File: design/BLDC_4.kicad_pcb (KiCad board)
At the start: 4 copper layers, 38.5 x 65 mm, 126 parts, among them K1 SERVO, P1 HALL/Encoder, P101 CANBUS, P2 SWD, P3 PWR_COMM, P4 IN+, P5 IN-, P6 MOTOR1, P7 MOTOR2, P9 MOTOR3, Q1 IRFS7530, Q2 IRFS7530, Q3 IRFS7530, Q4 IRFS7530, Q5 IRFS7530, Q6 IRFS7530, U1 STM32F40X_LQFP64, U2 TC2117, U3 DRV8302, U401 SN65HVD232, X1 MINI-USB-SHIELD-32005-201, X2 8MHz 10ppm

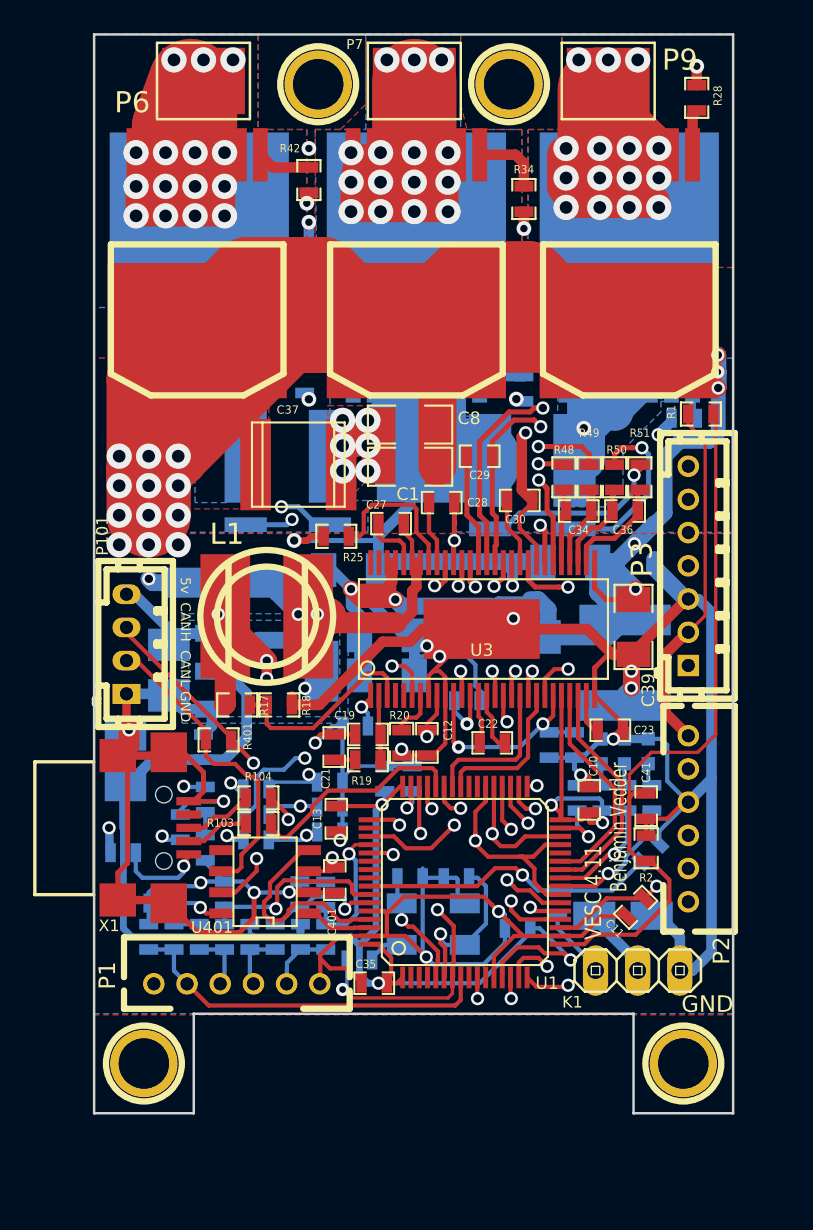
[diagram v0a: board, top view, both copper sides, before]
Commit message: Implemented some improvements in schematic, but layout is completely new.
Changes in schematic:
- 3.3V or 5V CAN transceiver can be used
- DRV8301 can also be used and configured via SPI
- JTAG connector changed
- Fixed pinning of P1
- Some additional decoupling and/or filtering of analog signals
- Improved buck design according TI Webench recommendation
- Changed some component values
- maybe others...

Changes in layout:
- completely new layout
- placement of the big components is unchanged
- CAN connector rotated by 180°
- kept one layer free as a good GND plane
- many traces should be shorter and have lower impedance now
- improved buck layout

Other changes:
- updated gerber files
- updated PDFs (schematic and component placement)
- deleted all outdated files except libraries and datasheets
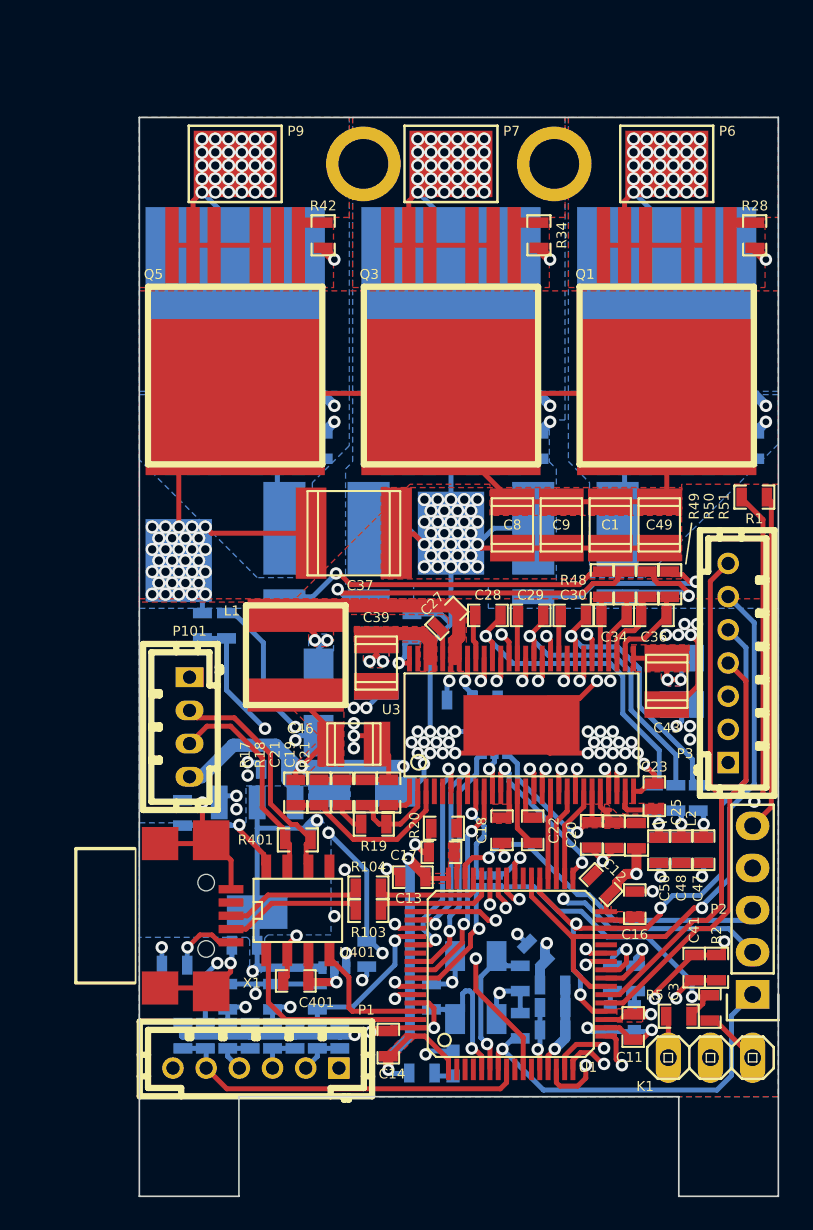
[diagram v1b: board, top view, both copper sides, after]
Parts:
- removed 1PIN (x2): P***, 1pin
- removed 1PIN (x2): P***, Connect:1pin
- removed C51: 15u, 100v, w_smd_cap:c_2220
- removed C52: 2.2u, CRF1:SMD-0603_c
- removed G***: oshw_silkscreen-back_3mm, oshw_silkscreen-back_3mm
- removed R30, R36, R46: 39k, CRF1:SMD-0603_r
- added C45: 6n8 opt, CRF1:SMD-0603_c, B.Cu at (97.7, 115.7)
- added C46: 47u,10V, w_smd_cap:c_1210, F.Cu at (94.2, 122.8)
- added C47: 100n, CRF1:SMD-0603_c, F.Cu at (115.2, 129.2)
- added C48: 100n, CRF1:SMD-0603_c, F.Cu at (113.9, 129.2)
- added C50: 100n, CRF1:SMD-0603_c, F.Cu at (112.5, 129.2)
- added JP1: JUMPER, open-project:S_JUMPER_2, B.Cu at (102.8, 131.0)
- added JP2: JUMPER, open-project:S_JUMPER_2, B.Cu at (101.8, 131.0)
- added JP3: JUMPER3, open-project:S_JUMPER_3, B.Cu at (102.6, 123.3)
- added JP4: JUMPER3, open-project:S_JUMPER_3, B.Cu at (93.0, 136.2)
- added L2: L, CRF1:SMD-0603_r, F.Cu at (111.2, 128.3)
- added L3: L, CRF1:SMD-0603_r, B.Cu at (106.1, 137.3)
- added R14: 0R, CRF1:SMD-0603_r, B.Cu at (100.5, 120.1)
- added REF**: MountingHole_3mm, Mounting_Holes:MountingHole_3mm, F.Cu at (106.8, 88.0)
- added REF**: MountingHole_3mm, Mounting_Holes:MountingHole_3mm, F.Cu at (94.2, 87.7)
- C1, C39, C40, C44, C8: value 10u,50V -> 10u,63V; footprint CRF1:SMD-1206 -> w_smd_cap:c_1210
- C10, C35, R25: moved to B.Cu
- C14, C16, C17, C3, R5: moved to F.Cu
- C18: value 2.2u -> 4.7u,25V; moved to F.Cu
- C19: value 120p -> 1p5
- C20: value 2.2u -> 2.2u,16V; moved to F.Cu
- C21: value 6.8n -> 2n
- C23: value 2.2u -> 2.2u,16V
- C25: value 100u -> 100n; footprint w_smd_cap:c_tant_B -> CRF1:SMD-0603_c; moved to F.Cu
- C33: value 100u -> 2.2u; footprint w_smd_cap:c_tant_B -> CRF1:SMD-0603_c
- C34, C36: value 2.2n -> 2n
- C37: value 15u,100V -> 22u,63V
- C43, C49, C9: value 10u,50V -> 10u,63V; footprint CRF1:SMD-1206 -> w_smd_cap:c_1210; moved to F.Cu
- D4: value DIODESCH -> Schottky; footprint Diodes_SMD:SMA_Handsoldering -> Diodes_SMD:SMA_Standard
- D5: footprint w_smd_diode:do214ac -> Diodes_SMD:SMA_Standard
- L1: value 22u -> 33u; footprint w_smd_inductors:inductor_smd_8x5mm -> pikim:inductor_smd_6x6mm
- P1: footprint CRF1:MICRO_JST_6 -> pikim:b6b-ph-kl
- P2: footprint CRF1:MICRO_JST_6 -> Pin_Headers:Pin_Header_Straight_1x05
- P3: footprint CRF1:b7b-ph-kl -> pikim:b7b-ph-kl
- Q1, Q2, Q3, Q4, Q5, Q6: footprint CRF1:D2PAK-7-GDS -> pikim:D2PAK-7-GDS
- R17: value 18k -> 52k5
- R18: value 3k3 -> 10k
- R19: value 15k -> 100k
- R21: value 220k -> 301k; moved to F.Cu
- R37, R38, R48, R49, R50, R51: value 100R -> 120R
- U3: value DRV8302 -> DRV8301/2; footprint CRF1:TSSOP-56-PP -> pikim:TSSOP-56-PP
- moved C25 29.8 mm to (109.8, 128.2), turned to 90 degrees
- moved P6 28.4 mm to (113.0, 87.8)
- moved R23 26.8 mm to (114.9, 126.0), turned to 270 degrees
- moved R26 25.3 mm to (113.5, 126.0), turned to 270 degrees
- moved R32 24.0 mm to (112.2, 126.0), turned to 270 degrees
- moved P9 23.0 mm to (87.0, 87.8)
- moved R24 22.6 mm to (115.2, 129.2), turned to 90 degrees
- moved R27 21.3 mm to (113.9, 129.2), turned to 90 degrees
- moved D3 20.8 mm to (100.1, 142.0)
- moved R33 20.2 mm to (112.5, 129.2), turned to 90 degrees
- moved C43 20.2 mm to (113.0, 119.0), turned to 90 degrees
- moved R22 19.8 mm to (98.2, 142.6), turned to 180 degrees
- moved C49 18.7 mm to (112.5, 109.5), turned to 90 degrees
- moved C44 18.0 mm to (113.9, 119.0), turned to 90 degrees
- moved R54 17.9 mm to (107.5, 112.8)
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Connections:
- C25 pad 1: VCC -> GND
- C25 pad 2: GND -> Net-(C25-Pad2)
- C31 pad 2: VCC -> Net-(C31-Pad2)
- C35 pad 2: VCC -> Net-(C31-Pad2)
- C401 pad 1: VCC -> Net-(C401-Pad1)
- D5 pad 1: GND -> +5V
- D5 pad 2: +5V -> GND
- P1 pad 1: +5V -> GND
- P1 pad 2: /Filters/TEMP_IN -> /Filters/HALL3_IN
- P1 pad 3: /Filters/HALL1_IN -> /Filters/HALL2_IN
- P1 pad 4: /Filters/HALL2_IN -> /Filters/HALL1_IN
- P1 pad 5: /Filters/HALL3_IN -> /Filters/TEMP_IN
- P1 pad 6: GND -> +5V
- P2 pad 1: VCC -> NRST
- P2 pad 3: GND -> SWDIO
- P2 pad 4: SWDIO -> GND
- P2 pad 5: NRST -> VCC
- Q1 pad S: /Mosfet driver/H1_VS -> /Mosfet driver/H3_VS
- Q2 pad D: /Mosfet driver/H1_VS -> /Mosfet driver/H3_VS
- Q2 pad S: /Mosfet driver/H1_LOW -> /Mosfet driver/H3_LOW
- Q5 pad S: /Mosfet driver/H3_VS -> /Mosfet driver/H1_VS
- Q6 pad D: /Mosfet driver/H3_VS -> /Mosfet driver/H1_VS
- Q6 pad S: /Mosfet driver/H3_LOW -> /Mosfet driver/H1_LOW
- R25 pad 1: GND -> Net-(R14-Pad1)
- R25 pad 2: Net-(R25-Pad2) -> GND
- R28 pad 2: /Mosfet driver/M_H1 -> /Mosfet driver/M_H3
- R29 pad 2: /Mosfet driver/M_L1 -> /Mosfet driver/M_L3
- R42 pad 2: /Mosfet driver/M_H3 -> /Mosfet driver/M_H1
- R43 pad 2: /Mosfet driver/M_L3 -> /Mosfet driver/M_L1
- R50 pad 2: Net-(C36-Pad1) -> Net-(C36-Pad2)
- R51 pad 2: Net-(C36-Pad2) -> Net-(C36-Pad1)
- R53 pad 1: GND -> /Mosfet driver/H1_LOW
- R53 pad 2: /Mosfet driver/H1_LOW -> GND
- R53 pad 3: /Mosfet driver/SH2_B -> /Mosfet driver/SH1_A
- R53 pad 4: /Mosfet driver/SH2_A -> /Mosfet driver/SH1_B
- R54 pad 1: /Mosfet driver/H3_LOW -> GND
- R54 pad 2: GND -> /Mosfet driver/H3_LOW
- R54 pad 3: /Mosfet driver/SH1_A -> /Mosfet driver/SH2_B
- R54 pad 4: /Mosfet driver/SH1_B -> /Mosfet driver/SH2_A
- U1 pad 11: Net-(U1-Pad11) -> (no net)
- U1 pad 13: VCC -> Net-(C31-Pad2)
- U1 pad 2: Net-(U1-Pad2) -> (no net)
- U1 pad 26: /MCU/BR_SO2 -> /Mosfet driver/BR_SO1
- U1 pad 28: Net-(U1-Pad28) -> (no net)
- U1 pad 3: Net-(U1-Pad3) -> (no net)
- U1 pad 39: Net-(U1-Pad39) -> (no net)
- U1 pad 4: Net-(U1-Pad4) -> (no net)
- U1 pad 50: Net-(U1-Pad50) -> /MCU/DRV_NSS
- U1 pad 54: Net-(U1-Pad54) -> (no net)
- U1 pad 55: Net-(U1-Pad55) -> /MCU/DRV_SCK
- U1 pad 56: Net-(U1-Pad56) -> /MCU/DRV_MISO
- U1 pad 57: /MCU/SERVO -> Net-(JP2-Pad1)
- U1 pad 9: Net-(U1-Pad9) -> (no net)
- U3 pad 10: GND -> /MCU/DRV_MISO
- U3 pad 11: Net-(C20-Pad2) -> Net-(JP3-Pad2)
- U3 pad 24: VCC -> Net-(C25-Pad2)
- U3 pad 25: /MCU/BR_SO1 -> /Mosfet driver/BR_SO1
- U3 pad 26: /MCU/BR_SO2 -> /MCU/BR_SO1
- U3 pad 30: Net-(C36-Pad2) -> Net-(C36-Pad1)
- U3 pad 31: Net-(C36-Pad1) -> Net-(C36-Pad2)
- U3 pad 4: Net-(U3-Pad4) -> (no net)
- U3 pad 49: Net-(R25-Pad2) -> Net-(R14-Pad1)
- U3 pad 5: Net-(U3-Pad5) -> (no net)
- U3 pad 55: Net-(U3-Pad55) -> (no net)
- U3 pad 8: GND -> /MCU/DRV_NSS
- U3 pad 9: VCC -> /MCU/DRV_MOSI
- U401 pad 3: VCC -> Net-(C401-Pad1)
- U401 pad 5: Net-(U401-Pad5) -> (no net)
- X1 pad 4: Net-(X1-Pad4) -> (no net)
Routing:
- net V_SUPPLY: track 290.3 -> 129.8 mm, vias 20 -> 36
- net /Mosfet driver/H3_VS: track 166.9 -> 66.0 mm, vias 18 -> 31
- net /Mosfet driver/H1_VS: track 150.6 -> 69.7 mm, vias 17 -> 31
- net /Mosfet driver/H2_VS: track 145.0 -> 65.1 mm, vias 17 -> 31
- net GND: track 397.8 -> 376.8 mm, vias 26 -> 106
- net /Mosfet driver/M_H1: track 49.8 -> 32.7 mm
- net /Mosfet driver/BR_SO1: track 0.00 -> 16.2 mm, vias 0 -> 2
- net /MCU/DRV_SCK: track 0.00 -> 14.8 mm, vias 0 -> 1
- net /Mosfet driver/H3_LOW: track 53.5 -> 39.5 mm
- net /MCU/BR_SO2: track 13.9 -> 0.00 mm
- net Net-(Q2-PadG): track 16.2 -> 2.80 mm
- net /MCU/DRV_MISO: track 0.00 -> 13.2 mm, vias 0 -> 2
- net /MCU/DRV_NSS: track 0.00 -> 12.8 mm, vias 0 -> 2
- net +5V: track 115.3 -> 103.5 mm
- net /MCU/L1: track 16.1 -> 5.31 mm, vias 2 -> 0
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- added copper zone on B.Cu, net +5V
- added copper zone on F.Cu, net +5V
- added copper zone on L2, net /Mosfet driver/H1_VS
- added copper zone on L3, net /Mosfet driver/H1_VS
- added copper zone on L2, net /Mosfet driver/H2_VS
- added copper zone on L3, net /Mosfet driver/H2_VS
- added copper zone on L2, net /Mosfet driver/H3_VS
- added copper zone on L3, net /Mosfet driver/H3_VS
- added copper zone on L2, net GND
- added copper zone on L3, net GND
- added copper zone on F.Cu, net Net-(C16-Pad1)
- added copper zone on F.Cu, net Net-(C17-Pad1)
- added copper zone on F.Cu, net Net-(C18-Pad1)
- added copper zone on F.Cu, net Net-(C20-Pad2)
- added copper zone on F.Cu, net Net-(C23-Pad2)
- added copper zone on F.Cu, net Net-(C25-Pad2)
- added copper zone on B.Cu, net Net-(C27-Pad1)
- added copper zone on F.Cu, net Net-(C27-Pad1)
- added copper zone on F.Cu, net VCC
- added copper zone on B.Cu, net V_SUPPLY
- removed copper zone on GND, net /Mosfet driver/H1_VS
- removed copper zone on GND2, net /Mosfet driver/H1_VS
- removed copper zone on GND, net /Mosfet driver/H2_VS
- removed copper zone on GND2, net /Mosfet driver/H2_VS
- removed copper zone on GND, net /Mosfet driver/H3_VS
- removed copper zone on GND2, net /Mosfet driver/H3_VS
- removed copper zone on GND, net GND
- removed copper zone on GND2, net GND
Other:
- net class Default: clearance 0.1778 -> 0.199999; trace_width 0.2032 -> 0.2; via_dia 0.8 -> 0.75; via_drill 0.5 -> 0.4
- rule trace_clearance: 0.1778 -> 0.199999
- rule trace_min: 0.2032 -> 0.2
- rule via_min_drill: 0.5 -> 0.4
- rule via_min_size: 0.8 -> 0.75
- board text added: "1"
- board text added: "2"
- board text added: "3"
- board text added: "5V"
- board text added: "GN"
- board text added: "RD"
- board text added: "SERVO"
- board text added: "VESC 4.11 pikim"
- board text removed: "3.3v"
- board text removed: "5v"
- board text removed: "VESC 4.11"

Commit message: Fixed some errors in v4.11p layout and gerber data. Increased revision to B.
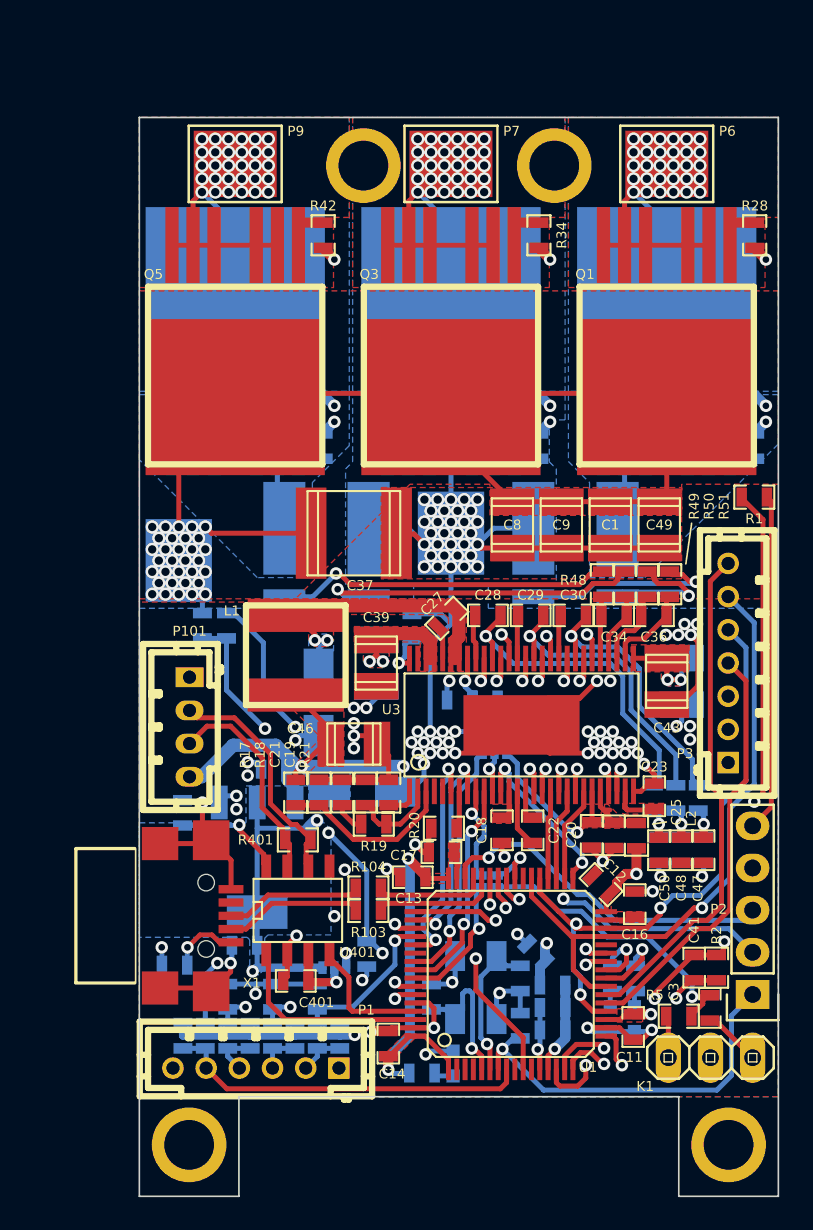
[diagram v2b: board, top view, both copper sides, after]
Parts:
- removed the REF** at (106.8, 88.0)
- removed the REF** at (94.2, 87.7)
- added REF**: MountingHole_3mm, Mounting_Holes:MountingHole_3mm, F.Cu at (116.7, 146.9)
- added REF**: MountingHole_3mm, Mounting_Holes:MountingHole_3mm, F.Cu at (84.2, 146.9)
- added REF**: MountingHole_3mm, Mounting_Holes:MountingHole_3mm, F.Cu at (106.2, 87.9)
- added REF**: MountingHole_3mm, Mounting_Holes:MountingHole_3mm, F.Cu at (94.7, 87.9)
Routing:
- added copper zone on L2, net V_SUPPLY
- added copper zone on L3, net V_SUPPLY
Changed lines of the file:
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@@
     (links 316)
     (no_connects 0)
-    (area 77.293999 82.524501 122.320359 150.050001)
+    (area 77.293999 82.774501 125.215045 152.876259)
     (thickness 1.6)
     (drawings 55)
     (tracks 1647)
     (zones 0)
-    (modules 130)
+    (modules 132)
     (nets 108)
   )
@@
   (title_block
     (title "BLDC Driver 4.11p")
-    (date 2016-01-06)
-    (rev A)
+    (date 2016-01-10)
+    (rev B)
     (company "Benjamin Vedder")
     (comment 1 "modified by pikim")
@@
     (add_net V_SUPPLY)
   )
+  (module Mounting_Holes:MountingHole_3mm (layer F.Cu)
+    (at 116.725 146.9)
+    (descr "Mounting hole, Befestigungsbohrung, 3mm, No Annular, Kein Restring,")
+    (tags "Mounting hole, Befestigungsbohrung, 3mm, No Annular, Kein Restring,")
+    (fp_text reference REF** (at 0 -4.0005) (layer F.SilkS) hide
+      (effects (font (size 1 1) (thickness 0.15)))
+    )
+    (fp_text value MountingHole_3mm (at 1.00076 5.00126) (layer F.Fab)
+      (effects (font (size 1 1) (thickness 0.15)))
+    )
+    (fp_circle (center 0 0) (end 3 0) (layer Cmts.User) (width 0.381))
+    (pad 4 thru_hole circle (at 0 0) (size 4.5 4.5) (drill 3) (layers *.Cu *.Mask))
+  )
+  (module Mounting_Holes:MountingHole_3mm (layer F.Cu)
+    (at 84.225 146.9)
+    (descr "Mounting hole, Befestigungsbohrung, 3mm, No Annular, Kein Restring,")
+    (tags "Mounting hole, Befestigungsbohrung, 3mm, No Annular, Kein Restring,")
+    (fp_text reference REF** (at 0 -4.0005) (layer F.SilkS) hide
+      (effects (font (size 1 1) (thickness 0.15)))
+    )
+    (fp_text value MountingHole_3mm (at 1.00076 5.00126) (layer F.Fab)
+      (effects (font (size 1 1) (thickness 0.15)))
+    )
+    (fp_circle (center 0 0) (end 3 0) (layer Cmts.User) (width 0.381))
+    (pad 3 thru_hole circle (at 0 0) (size 4.5 4.5) (drill 3) (layers *.Cu *.Mask))
+  )
+  (module Mounting_Holes:MountingHole_3mm (layer F.Cu)
+    (at 106.225 87.9)
+    (descr "Mounting hole, Befestigungsbohrung, 3mm, No Annular, Kein Restring,")
+    (tags "Mounting hole, Befestigungsbohrung, 3mm, No Annular, Kein Restring,")
+    (fp_text reference REF** (at 0 -4.0005) (layer F.SilkS) hide
+      (effects (font (size 1 1) (thickness 0.15)))
+    )
+    (fp_text value MountingHole_3mm (at 1.00076 5.00126) (layer F.Fab)
+      (effects (font (size 1 1) (thickness 0.15)))
+    )
+    (fp_circle (center 0 0) (end 3 0) (layer Cmts.User) (width 0.381))
+    (pad 2 thru_hole circle (at 0 0) (size 4.5 4.5) (drill 3) (layers *.Cu *.Mask))
+  )
+  (module Mounting_Holes:MountingHole_3mm (layer F.Cu)
+    (at 94.725 87.9)
+    (descr "Mounting hole, Befestigungsbohrung, 3mm, No Annular, Kein Restring,")
+    (tags "Mounting hole, Befestigungsbohrung, 3mm, No Annular, Kein Restring,")
+    (fp_text reference REF** (at 0 -4.0005) (layer F.SilkS) hide
+      (effects (font (size 1 1) (thickness 0.15)))
+    )
+    (fp_text value MountingHole_3mm (at 1.00076 5.00126) (layer F.Fab)
+      (effects (font (size 1 1) (thickness 0.15)))
+    )
+    (fp_circle (center 0 0) (end 3 0) (layer Cmts.User) (width 0.381))
+    (pad 1 thru_hole circle (at 0 0) (size 4.5 4.5) (drill 3) (layers *.Cu *.Mask))
+  )
   (module pikim:b6b-ph-kl (layer F.Cu)
     (at 88.25 142.275 180)
@@
       (net 58 "/Mosfet driver/SH1_B"))
   )
-  (module Mounting_Holes:MountingHole_3mm (layer F.Cu)
-    (at 106.775 88)
-    (descr "Mounting hole, Befestigungsbohrung, 3mm, No Annular, Kein Restring,")
-    (tags "Mounting hole, Befestigungsbohrung, 3mm, No Annular, Kein Restring,")
-    (fp_text reference REF** (at 0 -4.0005) (layer F.SilkS) hide
-      (effects (font (size 1 1) (thickness 0.15)))
-    )
-    (fp_text value MountingHole_3mm (at 1.00076 5.00126) (layer F.Fab)
-      (effects (font (size 1 1) (thickness 0.15)))
-    )
-    (fp_circle (center 0 0) (end 3 0) (layer Cmts.User) (width 0.381))
-    (pad 1 thru_hole circle (at -0.55 -0.2) (size 4.5 4.5) (drill 3) (layers *.Cu *.Mask))
-  )
   (module Pin_Headers:Pin_Header_Straight_1x05 (layer F.Cu)
     (at 118.175 137.84 180)
@@
     )
   )
-  (module Mounting_Holes:MountingHole_3mm (layer F.Cu)
-    (at 94.175 87.65)
-    (descr "Mounting hole, Befestigungsbohrung, 3mm, No Annular, Kein Restring,")
-    (tags "Mounting hole, Befestigungsbohrung, 3mm, No Annular, Kein Restring,")
-    (fp_text reference REF** (at 0 -4.0005) (layer F.SilkS) hide
-      (effects (font (size 1 1) (thickness 0.15)))
-    )
-    (fp_text value MountingHole_3mm (at 1.00076 5.00126) (layer F.Fab)
-      (effects (font (size 1 1) (thickness 0.15)))
-    )
-    (fp_circle (center 0 0) (end 3 0) (layer Cmts.User) (width 0.381))
-    (pad 1 thru_hole circle (at 0.55 0.15) (size 4.5 4.5) (drill 3) (layers *.Cu *.Mask))
-  )
   (module open-project:S_JUMPER_3 (layer B.Cu)
     (at 92.975 136.225)
@@
       )
     )
+  )
+  (zone (net 40) (net_name V_SUPPLY) (layer L2) (hatch edge 0.508)
+    (priority 1)
+    (connect_pads yes (clearance 0.2))
+    (min_thickness 0.2)
+    (fill yes (arc_segments 16) (thermal_gap 0.508) (thermal_bridge_width 0.508))
+    (polygon
+      (pts
+        (xy 81.475 109.15) (xy 85.725 109.15) (xy 85.725 114.25) (xy 81.475 114.25)
+      )
+    )
+  )
+  (zone (net 40) (net_name V_SUPPLY) (layer L3) (hatch edge 0.508)
+    (priority 1)
+    (connect_pads yes (clearance 0.2))
+    (min_thickness 0.2)
+    (fill yes (arc_segments 16) (thermal_gap 0.508) (thermal_bridge_width 0.508))
+    (polygon
+      (pts
+        (xy 81.475 109.15) (xy 85.725 109.15) (xy 85.725 114.25) (xy 81.475 114.25)
+      )
+    )
+  )
+  (zone (net 2) (net_name GND) (layer L2) (hatch edge 0.508)
+    (priority 1)
+    (connect_pads yes (clearance 0.2))
+    (min_thickness 0.2)
+    (fill yes (arc_segments 16) (thermal_gap 0.508) (thermal_bridge_width 0.508))
+    (polygon
+      (pts
+        (xy 97.875 107.5) (xy 102.125 107.5) (xy 102.125 112.6) (xy 97.875 112.6)
+      )
+    )
+  )
+  (zone (net 2) (net_name GND) (layer L3) (hatch edge 0.508)
+    (priority 1)
+    (connect_pads yes (clearance 0.2))
+    (min_thickness 0.2)
+    (fill yes (arc_segments 16) (thermal_gap 0.508) (thermal_bridge_width 0.508))
+    (polygon
+      (pts
+        (xy 97.875 107.5) (xy 102.125 107.5) (xy 102.125 112.6) (xy 97.875 112.6)
+      )
+    )
